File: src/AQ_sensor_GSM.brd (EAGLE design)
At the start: 110 x 64 mm, 49 parts, among them IC2 MCP73831/OT, J1 F-1X03-SIP-100-32, SW1 PCM12SMTR, SW2 PCM12SMTR, U2 TEXAS_INSTRUMENTS_SN74HC125TE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, U3 TEXAS_INSTRUMENTS_LM1117IMP-3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, X1 53048-08, X2 SIMLOCK-C707_10M006_512_2, X4 50 Ohms

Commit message: created src folder
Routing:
- net GND: vias 99 -> 103
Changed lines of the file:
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@@
 <via x="39.9" y="4.4" extent="1-16" drill="0.35"/>
 <via x="39.9" y="2.8" extent="1-16" drill="0.35"/>
-<wire x1="15.825" y1="8.84" x2="15.825" y2="5.03" width="0" layer="19" extent="1-1"/>
+<via x="15" y="11.5" extent="1-16" drill="0.35"/>
+<via x="16.2" y="11.5" extent="1-16" drill="0.35"/>
+<via x="19.5" y="10.9" extent="1-16" drill="0.35"/>
+<via x="19.5" y="9.6" extent="1-16" drill="0.35"/>
 </signal>
 <signal name="+5V" class="1">

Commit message: sorted DRC
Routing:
- net N$12: track 20.0 -> 22.3 mm
- net +5V: track 265.7 -> 264.9 mm
- net 2.8V: track 12.7 -> 12.1 mm
- net +3V3: track 67.8 -> 67.2 mm
- net DHT_OUT: track 25.8 -> 25.3 mm

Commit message: Organized schematic
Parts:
- removed H1, H2, H3, H4: MOUNT-PAD-ROUND2.8, AQ_sensor_GSM:2,8-PAD
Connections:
- net GND: no longer H1.B2,8, H2.B2,8, H3.B2,8, H4.B2,8
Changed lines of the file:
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@@
 <attribute name="VALUE" x="87.925" y="33.665" size="1.27" layer="28" rot="MR270"/>
-</element>
-<element name="H1" library="AQ_sensor_GSM" library_urn="urn:adsk.eagle:library:30300195" package="2,8-PAD" package3d_urn="urn:adsk.eagle:package:30300289/1" value="MOUNT-PAD-ROUND2.8" x="106" y="4" smashed="yes">
-<attribute name="POPULARITY" value="6" x="106" y="4" size="1.778" layer="27" display="off"/>
-</element>
-<element name="H2" library="AQ_sensor_GSM" library_urn="urn:adsk.eagle:library:30300195" package="2,8-PAD" package3d_urn="urn:adsk.eagle:package:30300289/1" value="MOUNT-PAD-ROUND2.8" x="106" y="60" smashed="yes">
-<attribute name="POPULARITY" value="6" x="106" y="60" size="1.778" layer="27" display="off"/>
-</element>
-<element name="H3" library="AQ_sensor_GSM" library_urn="urn:adsk.eagle:library:30300195" package="2,8-PAD" package3d_urn="urn:adsk.eagle:package:30300289/1" value="MOUNT-PAD-ROUND2.8" x="4" y="60" smashed="yes">
-<attribute name="POPULARITY" value="6" x="4" y="60" size="1.778" layer="27" display="off"/>
-</element>
-<element name="H4" library="AQ_sensor_GSM" library_urn="urn:adsk.eagle:library:30300195" package="2,8-PAD" package3d_urn="urn:adsk.eagle:package:30300289/1" value="MOUNT-PAD-ROUND2.8" x="4" y="4" smashed="yes">
-<attribute name="POPULARITY" value="6" x="4" y="4" size="1.778" layer="27" display="off"/>
 </element>
 <element name="DHT" library="led" library_urn="urn:adsk.eagle:library:259" package="CHIP-LED0603" package3d_urn="urn:adsk.eagle:package:15819/3" value="GREEN" x="52.54416875" y="5.7942" smashed="yes">
@@
 <contactref element="X1" pad="7"/>
 <contactref element="C1" pad="2"/>
-<contactref element="H1" pad="B2,8"/>
-<contactref element="H2" pad="B2,8"/>
-<contactref element="H3" pad="B2,8"/>
-<contactref element="H4" pad="B2,8"/>
 <contactref element="SV2" pad="2"/>
 <contactref element="DHT" pad="C"/>

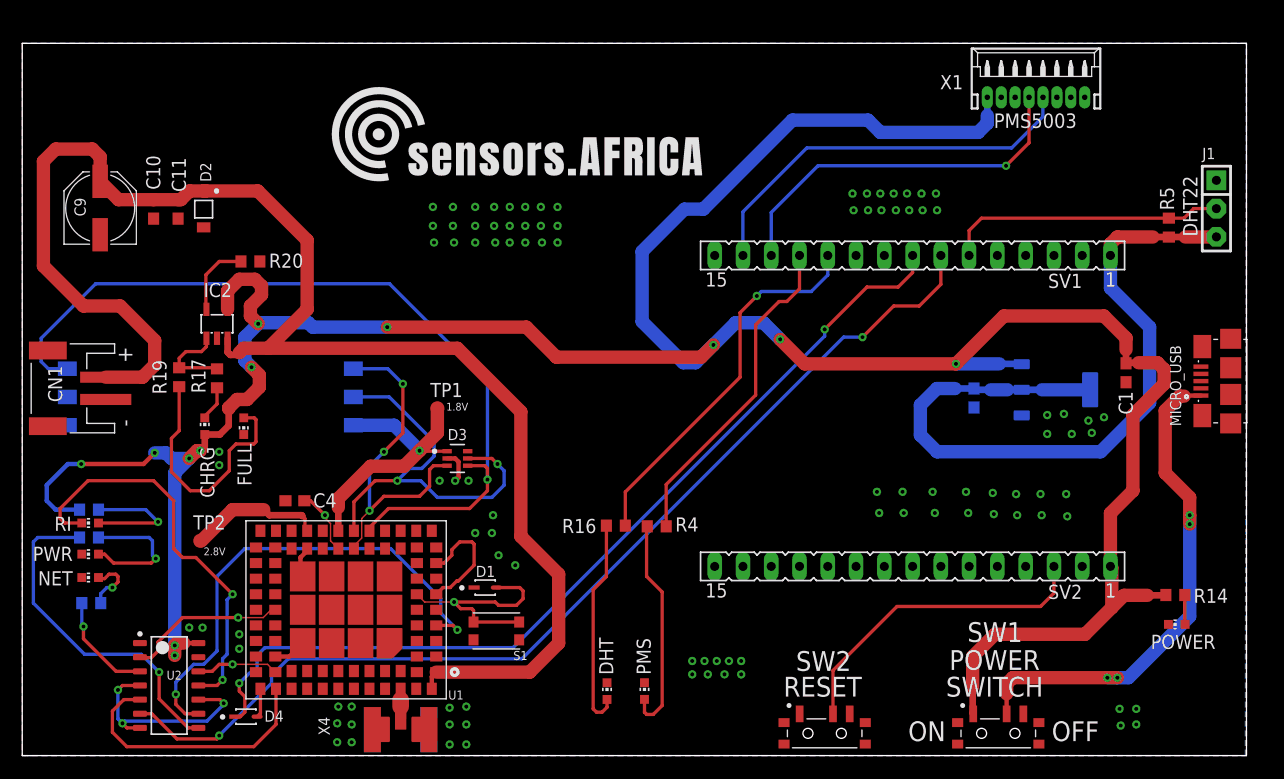
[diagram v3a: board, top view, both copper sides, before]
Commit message: Feature: Change components' positions.
1. Rotate NodeMCU 90 degrees anti-clockwise. 2. Add  onboard GSM Antenna. 3. Move Simcard Holder to top Layer. 4. Change Reset button to push button. 5. Rearrange Charging Circuitry layout to minimise trace resistance.
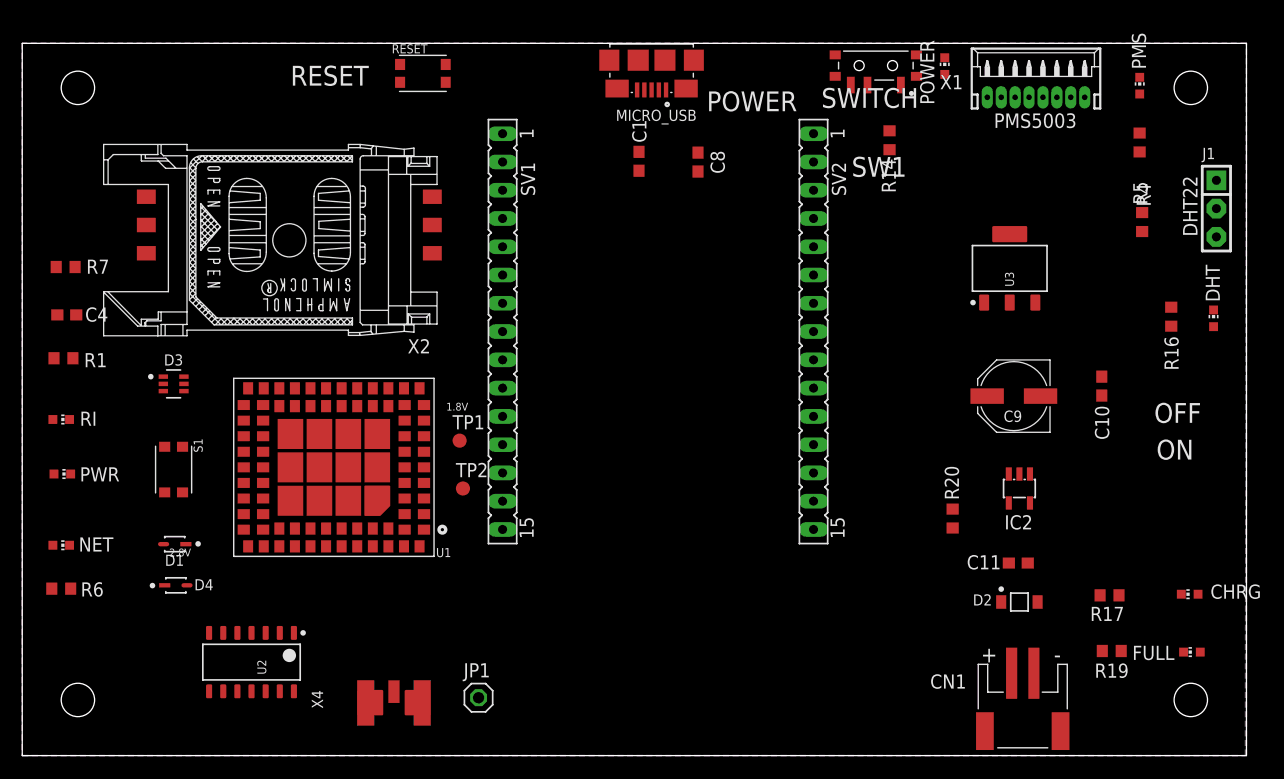
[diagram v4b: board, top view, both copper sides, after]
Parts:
- removed SW2: PCM12SMTR, AQ_sensor_GSM:SW_PCM12SMTR
- added JP1: PINHD-1X1, Connector:1X01
- added RESET: KMR621NGLFS, KMR621NGLFS:SW_KMR621NGLFS
- moved CN1 90.9 mm to (89.9, 3.70), turned to 180 degrees
- moved CHRG 89.8 mm to (104.9, 14.5), turned to 90 degrees
- moved FULL 87.6 mm to (105.1, 9.30), turned to 90 degrees
- moved R19 87.3 mm to (97.9, 9.40), turned to 180 degrees
- moved C10 86.7 mm to (97.0, 33.2), turned to 90 degrees
- moved C9 83.8 mm to (89.1, 32.3), turned to 180 degrees
- moved R17 82.5 mm to (97.7, 14.4), turned to 180 degrees
- moved C11 81.9 mm to (89.5, 17.3), turned to 0 degrees
- moved D2 81.4 mm to (89.6, 13.8), turned to 0 degrees
- moved IC2 73.6 mm to (89.6, 24.0), turned to 180 degrees
- moved PMS 70.3 mm to (100.4, 60.2)
- moved R20 67.2 mm to (83.6, 21.3), turned to 90 degrees
- moved DHT 64.0 mm to (107.0, 39.3)
- moved SW1 61.0 mm to (76.7, 62.0), turned to 180 degrees
- moved MICRO_USB 55.9 mm to (56.5, 59.8), turned to 180 degrees
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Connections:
- net ESP_RST: now also RESET.1_1, RESET.1_2; no longer SW2.2
- net GND: now also RESET.2_1, RESET.2_2; no longer SW2.1, SW2.S1, SW2.S2, SW2.S3, SW2.S4
- net GSM_ANT: now also JP1.1
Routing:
- net +5V: track 264.9 -> 0.00 mm, vias 12 -> 0
- net V_LIPO: track 136.5 -> 0.00 mm
- net GSM_TX_5V: track 92.9 -> 0.00 mm, vias 2 -> 0
- net GSM_RX_O: track 82.4 -> 0.00 mm, vias 2 -> 0
- net SIMDATA: track 75.4 -> 0.00 mm, vias 1 -> 0
- net +3V3: track 67.2 -> 0.00 mm
- net VIN: track 46.5 -> 0.00 mm, vias 4 -> 0
- net PWRSTAT: track 44.4 -> 0.00 mm, vias 2 -> 0
- net GND: track 39.1 -> 0.00 mm, vias 103 -> 0
- net SIMRST: track 37.4 -> 0.00 mm, vias 2 -> 0
- net RI_5V: track 36.7 -> 0.00 mm, vias 2 -> 0
- net PMS_TX: track 36.2 -> 0.00 mm
- net DHT_LED: track 34.5 -> 0.00 mm, vias 1 -> 0
- net PMS_RX: track 33.7 -> 0.00 mm, vias 1 -> 0
- net SIMCLK: track 31.2 -> 0.00 mm, vias 3 -> 0
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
